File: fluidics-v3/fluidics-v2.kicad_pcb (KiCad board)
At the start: 4 copper layers, 85 x 95.5 mm, 83 parts, among them IC2 ADUM1250WSRZ-RL7, J1 PJ-063AH, J10 87832-0410, J11 0705430001, J12 87832-0410, J13 0705430001, J14 87832-0410, J15 0533980671, J16 0705430001, J17 0533980671, J18 87832-0410, J19 0705430001, J2 B6B-ZR-SM4-TF, J20 0533980671, J21 87832-0410, J22 0705430001, J24 0705430001, J25 87832-0410, J3 A-DS_15_A_KG-T4S, J4 B6B-ZR-SM4-TF, J5 Screw_Terminal_01x06, J6 Socket_1x24_2.54mm_SMT, J7 Socket_1x24_2.54mm_SMT, U1 TPL7407LDR, U11 MAX3221, U12 CD4050BDR, U13 TC7PZ17FU, U3 AP7366EA-33W5-7, U4 D24V10FX, U6 LTC4311CSC6-TRPBF

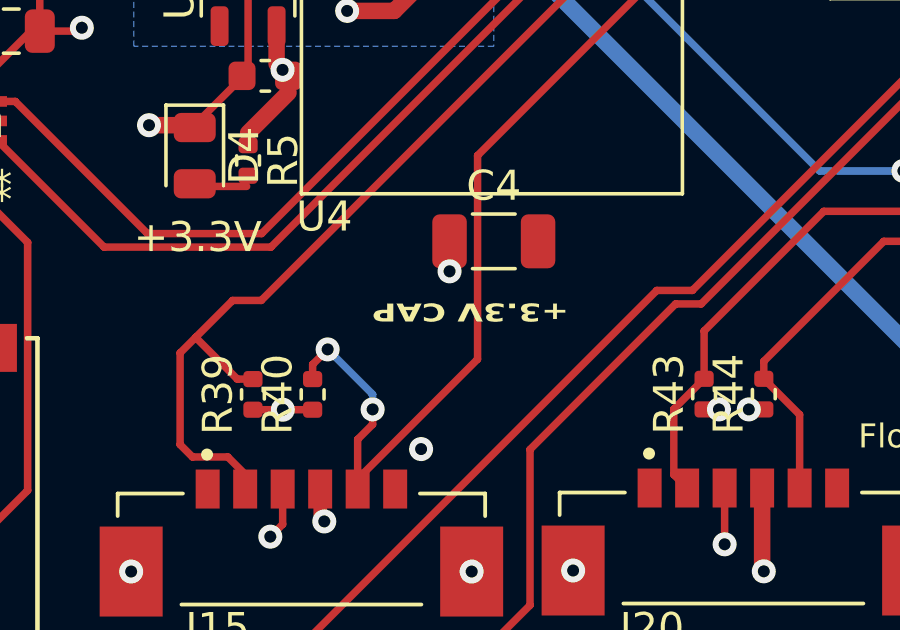
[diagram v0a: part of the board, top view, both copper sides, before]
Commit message: DNP the orphaned LTC4311, clean the CPL, fix undersized silk text
U6 (LTC4311 I2C accelerator) and R1 (0R) are vestigial from the accelerator
removal and cannot work as placed: pcbnew connectivity shows U6.1/U6.3 are the
only two of the twenty +5V pads unreachable from the buck output U4.5, and the
bus pins connect solely to each other -- Net-(U6-BUS1) = {U6.6, R1.1},
Net-(U6-BUS2) = {U6.4, R1.2}. Marked DNP on both the schematic (svalves sheet)
and the board rather than deleted, so the copper is left untouched and the
choice is reversible; deleting both is the cleaner fix for a future revision.

H2/H3/H4 (mounting holes) and TP1/TP2/TP3 (test points) are not placeable
parts but were being emitted into the placement file. Marked exclude-from-
position-files. Position export now also passes --exclude-dnp, so the CPL
drops from 82 to 74 rows and contains only parts a machine actually places.

Silk text "+3.3V CAP" was 0.8 x 0.6 mm against the board's own 0.8 mm silk
minimum; height raised to 0.8 mm. DRC text_height 1 -> 0, no other violation
moved.

Verified after the change: 44/44 socket pins still on the correct net, 4/4
intended no-connects, DRC unconnected 6 (unchanged baseline), schematic parity
0, 0 electrical violations, cosmetic 85 -> 84. Fab package regenerated.

Co-Authored-By: Claude Opus 5 (1M context) <noreply@anthropic.com>
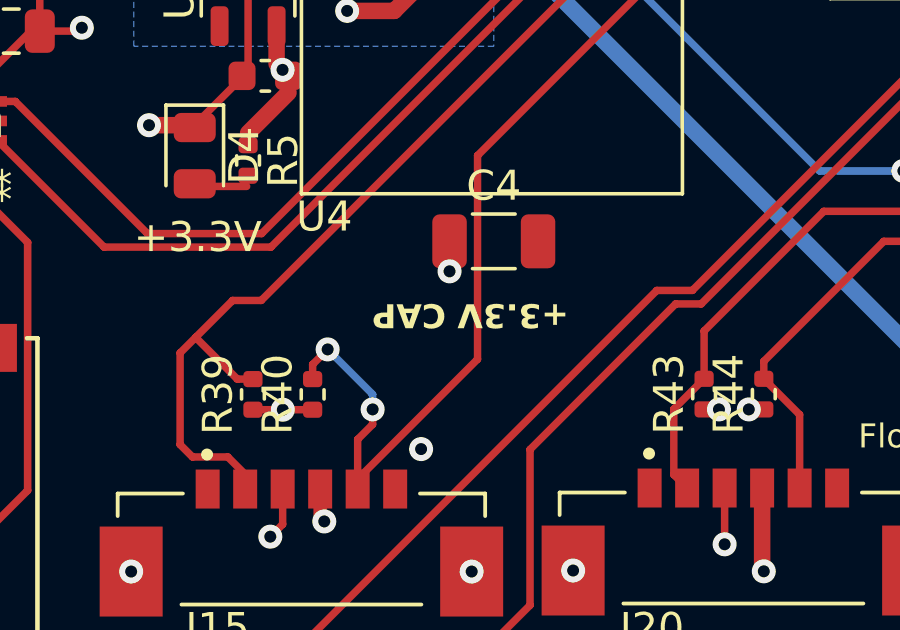
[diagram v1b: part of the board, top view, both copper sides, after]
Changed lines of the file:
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@@
 			)
 		)
+		(attr exclude_from_pos_files)
 		(duplicate_pad_numbers_are_jumpers no)
 		(fp_circle
@@
 			)
 		)
+		(attr exclude_from_pos_files)
 		(duplicate_pad_numbers_are_jumpers no)
 		(fp_circle
@@
 			)
 		)
+		(attr exclude_from_pos_files)
 		(duplicate_pad_numbers_are_jumpers no)
 		(fp_line
@@
 			)
 		)
-		(attr smd)
+		(attr smd dnp)
 		(duplicate_pad_numbers_are_jumpers no)
 		(fp_line
@@
 			)
 		)
+		(attr exclude_from_pos_files)
 		(duplicate_pad_numbers_are_jumpers no)
 		(fp_line
@@
 			)
 		)
-		(attr smd)
+		(attr smd dnp)
 		(duplicate_pad_numbers_are_jumpers no)
 		(fp_line
@@
 			)
 		)
+		(attr exclude_from_pos_files)
 		(duplicate_pad_numbers_are_jumpers no)
 		(fp_line
@@
 			)
 		)
+		(attr exclude_from_pos_files)
 		(duplicate_pad_numbers_are_jumpers no)
 		(fp_circle
@@
 		)
 	)
-	(gr_text "+3.3V CAP"
-		(at 159 92 180)
-		(layer "F.SilkS")
-		(effects
-			(font
-				(size 0.6 0.8)
-				(thickness 0.15)
-				(bold yes)
-			)
-			(justify left bottom)
-		)
-	)
 	(gr_text "Selector Valves"
 		(at 129 67 0)
@@
 		)
 	)
+	(gr_text "+3.3V CAP"
+		(at 159 92 180)
+		(layer "F.SilkS")
+		(effects
+			(font
+				(size 0.8 0.8)
+				(thickness 0.16)
+				(bold yes)
+			)
+			(justify left bottom)
+		)
+	)
 	(gr_text "J10"
 		(at 110.825 52 90)
@@
 	)
 	(segment
+		(start 184.2 60.22)
+		(end 187.5 60.22)
+		(width 0.25)
+		(layer "F.Cu")
+		(net "/POT_ANALOG")
+	)
+	(segment
 		(start 184.2 52.6)
 		(end 187.5 52.6)
@@
 		(net "/Bubble Sensors/Calib 1 5V")
 	)
-	(segment
-		(start 184.2 60.22)
-		(end 187.5 60.22)
-		(width 0.25)
-		(layer "F.Cu")
-		(net "/POT_ANALOG")
-	)
 	(zone

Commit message: Set socket MPN to Samtec SSM-124-L-SV
The land pattern was generated from Harwin's M20-786, but that series stops at
20 ways -- so no single Harwin part ever covered a row, and the board has never
had a one-part socket solution. Samtec's SSM-124-L-SV is a real 24-position
single-row 2.54mm SMT socket, and its footprint matches this land:

  tails         alternating          <- same
  offset        1.6025 mm            <- board has 1.65 mm, 47 um difference
  pad           1.905 x 1.02 mm      <- board has 1.9 x 1.0 mm
  pitch / span  2.54 / 58.42 mm      <- identical

Verified against the vendor footprint (SAMTEC_SSM-124-L-SV.kicad_mod). No
copper change: the tail sits 47 um off pad centre on a 1.9 mm pad. The
dual-land footprint is kept, so Harwin strips remain an alternative.

Value set on both the schematic and the board so BOM and CPL agree. Re-checked
after: 44/44 socket pins on the correct net, 4/4 intended no-connects, DRC
unconnected 6 (baseline), parity 0, 0 electrical violations. Fab package
regenerated.

Note: SSM-124-L-SV-P is the same socket with a pick-and-place pad, needed if
the sockets are to be machine placed rather than hand fitted. Only the plain
variant's land was verified here.

Co-Authored-By: Claude Opus 5 (1M context) <noreply@anthropic.com>
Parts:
- J6, J7: value Socket_1x24_2.54mm_SMT -> SSM-124-L-SV
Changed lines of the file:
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@@
 			)
 		)
-		(property "Value" "Socket_1x24_2.54mm_SMT"
+		(property "Value" "SSM-124-L-SV"
 			(at 0 32.08 0)
 			(layer "F.Fab")
@@
 			)
 		)
-		(property "Value" "Socket_1x24_2.54mm_SMT"
+		(property "Value" "SSM-124-L-SV"
 			(at 0 32.08 0)
 			(layer "F.Fab")

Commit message: U3: swap AP7366EA-33W5-7 -> AP2112K-3.3TRG1
Pin-compatible drop-in for the +3.3V LDO. Both parts are 600mA CMOS
LDOs with enable in SOT-23-5, and the fixed-output pin assignment is
identical (1=IN, 2=GND, 3=EN, 4=NC, 5=OUT), matching the board wiring
(+5V / GND / +5V / no-connect / +3.3V). Footprint unchanged
(Package_TO_SOT_SMD:SOT-23-5), so no layout impact.

Schematic, PCB and both BOMs updated together; schematic parity 0,
DRC 0 errors. Value text is on F.Fab only, so the existing gerbers and
positions.csv remain valid and were not regenerated.

Note: order the FIXED 3.3V variant. On the ADJ version pin 4 is the
feedback pin, not a no-connect.

Co-Authored-By: Claude Opus 5 (1M context) <noreply@anthropic.com>
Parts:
- U3: value AP7366EA-33W5-7 -> AP2112K-3.3TRG1
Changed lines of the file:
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@@
 			)
 		)
-		(property "Value" "AP7366EA-33W5-7"
+		(property "Value" "AP2112K-3.3TRG1"
 			(at 0 2.4 90)
 			(layer "F.Fab")

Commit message: U4: replace Pololu D24V10FX with Traco TSR1-2450E, drop 5V power-good
Swap the 24V->5V step-down for a Traco TSR 1-2450E (SIP-3, through-hole,
1A) using the stock KiCad symbol/footprint pair. The TSR is a 3-pin part,
so the Pololu's PG and nSHDN pins go away; nSHDN was already unconnected.

Schematic:
- psu: U4 -> Converter_DCDC:TSR1-2450E on
  Converter_DCDC:Converter_DCDC_TRACO_TSR1-xxxxE_THT
- Remove the PG-5V hierarchical label, sheet pin, wire stub and the 47k
  pull-up R51; PG-5V no longer exists as a net
- No-connect flags on J7 pin 1 and U2 pin 25, freeing Teensy pin 33

PCB:
- Place U4 at (156.437, 71.905) rot +90 so Vin lands on the existing +24V
  arrival node; GND and Vout follow on the 2.54mm pitch. Rotating rather
  than mirroring keeps the TSR body clear of R3 and D2, which the part
  would otherwise sit on top of.
- Route +5V on F.Cu 0.55mm from the existing tap across to Vout, plus a
  via restoring the F.Cu/B.Cu junction the old through-hole pad provided
- Remove orphaned PG-5V copper (16 segments, 2 vias) and the now-dead
  6-segment +3.3V run that used to feed R51

DRC: 0 errors, schematic parity clean, unconnected 7 -> 6.
Courtyard overlaps 2 -> 0, dangling tracks 4 -> 0. ERC 33 -> 31.
One cosmetic silkscreen warning remains: the "24V->5V Module" board label
now overlaps U4's outline and wants nudging by hand.

Co-Authored-By: Claude Opus 5 (1M context) <noreply@anthropic.com>
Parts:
- removed R51: 47k, Resistor_SMD:R_0603_1608Metric_Pad0.98x0.95mm_HandSolder
- U4: value D24V10FX -> TSR1-2450E; footprint pololu:D24V10FX -> Converter_DCDC:Converter_DCDC_TRACO_TSR1-xxxxE_THT
- moved U4 7.62 mm to (156.4, 71.9), turned to 90 degrees
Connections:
- J7 pad 1: /PG-5V -> unconnected-(J7-Pin_1-Pad1)
- U4 pad 1: /PG-5V -> +24V
- U4 pad 2: unconnected-(U4-nSHDN-Pad2) -> GND
- U4 pad 3: +24V -> +5V
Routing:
- net /PG-5V: track 49.0 -> 0.00 mm, vias 2 -> 0
- net +3.3V: track 68.6 -> 50.2 mm
- net +5V: track 99.1 -> 112.4 mm, vias 6 -> 7

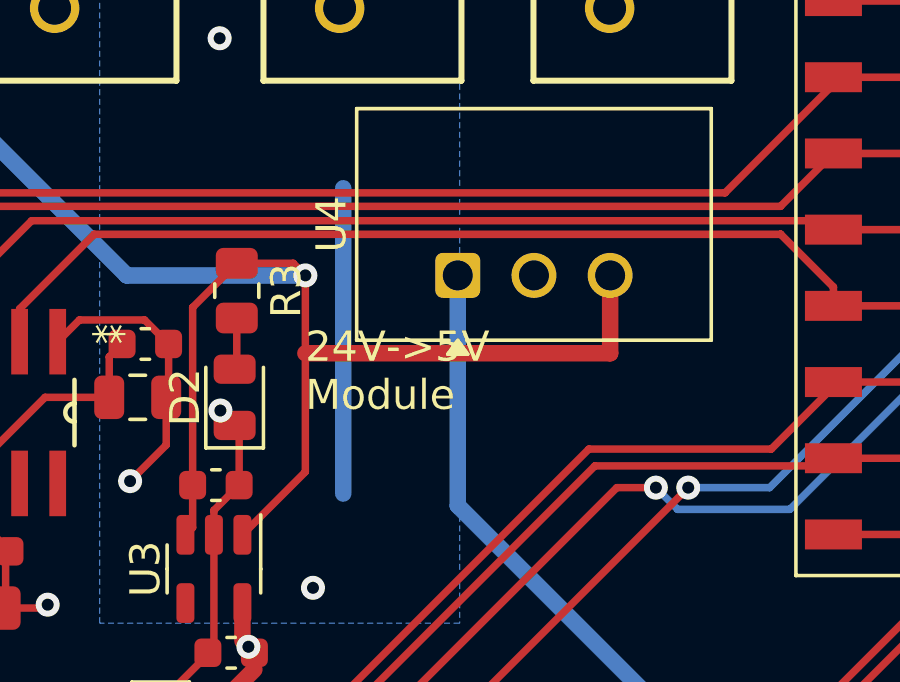
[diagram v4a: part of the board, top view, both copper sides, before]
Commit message: v3: finish TSR regulator swap, reconcile BOM, regenerate fab outputs
Follow-up to a773dae, which replaced the Pololu D24V10FX with a Traco
TSR 1-2450E. Completes the board cleanup and brings the fabrication
package back in step with the design.

Board:
- Remove the redundant B.Cu 3.3V spine at x=152.62; the 3V3_bridge_Bcu
  zone already carried that path, so connectivity is unchanged
- Move the "24V->5V Module" silk label clear of U4's outline
- R10 42K -> 47K. 42k is not an E24 value; R4 already uses 47k on the
  same +24V rail feeding an identical indicator LED, and the current
  difference is 0.52mA vs 0.47mA

DRC 0 errors, schematic parity clean, 6 unconnected items (all
pre-existing). Courtyard overlaps and dangling tracks both at 0.

Fabrication outputs, all regenerated from the current board:
- gerbers/ + drill (4-layer, metric 4.6, X2, merged PTH/NPTH), rezipped
- positions.csv, netlist.ipc, fluidics-v3.step

BOM and CPL:
- Add fluidics-v3-bom.xlsx, flattened from the EasyEDA template that
  broke JLC's importer: header moved to row 1, dropping five preamble
  rows, merged cells A1:D5, an embedded logo, =ROW() formulas whose
  cached values were lost on re-save, and four phantom trailing rows.
  Supplier Part renamed to "LCSC Part #" for auto-detection.
- Reconcile it against the board: add U4 (TSR 1-2450E, C5346721), drop
  R51 from the R10,R51 group (the PG pull-up died with the power-good
  net), correct U3 to AP2112K-3.3TRG1 / C51118 (was still the
  AP7366EA-33W5-7 part number from before 864ac36)
- Add cpl_jlcpcb.csv in JLCPCB column format
- Remove bom.csv: superseded, no LCSC column, and its range notation
  (C15-C17, R39-R44) is unparseable by JLC

BOM and CPL now agree exactly: 74 designators, 74 rows, no mismatch in
either direction, every line carrying an LCSC part number.

Co-Authored-By: Claude Opus 5 (1M context) <noreply@anthropic.com>
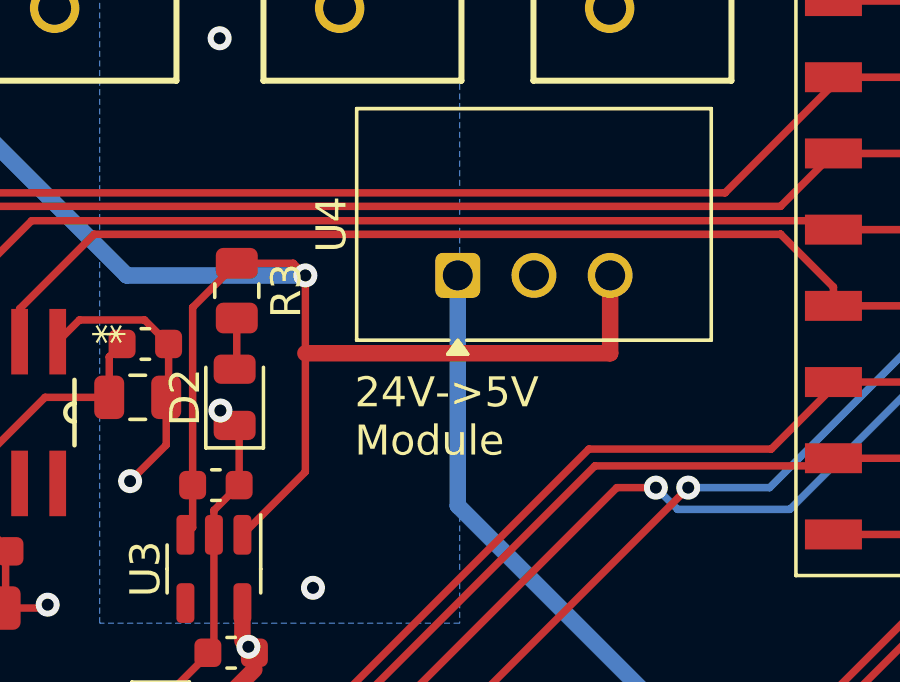
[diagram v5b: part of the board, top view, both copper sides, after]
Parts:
- R10: value 42K -> 47K
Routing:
- net +3.3V: track 50.2 -> 40.0 mm
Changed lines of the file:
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@@
 			)
 		)
-		(property "Value" "42K"
+		(property "Value" "47K"
 			(at 0 1.43 0)
 			(layer "F.Fab")
@@
 			(net "unconnected-(J7-Pin_1-Pad1)_1")
 			(pinfunction "Pin_1_1")
-			(pintype "passive")
+			(pintype "passive+no_connect")
 		)
 		(pad "1" smd rect
@@
 			(net "unconnected-(J7-Pin_1-Pad1)")
 			(pinfunction "Pin_1_1")
-			(pintype "passive")
+			(pintype "passive+no_connect")
 		)
 		(pad "2" smd rect
@@
 		)
 	)
-	(gr_text "24V->5V \nModule"
-		(at 151.35728 76.477 0)
+	(gr_text "+24V IN"
+		(at 153 37 0)
 		(layer "F.SilkS")
 		(effects
@@
 		)
 	)
-	(gr_text "+24V IN"
-		(at 153 37 0)
+	(gr_text "24V->5V \nModule"
+		(at 153 78 0)
 		(layer "F.SilkS")
 		(effects
@@
 		(net "+3.3V")
 	)
-	(segment
-		(start 152.61968 69)
-		(end 152.61968 79.17572)
-		(width 0.55)
-		(layer "B.Cu")
-		(net "+3.3V")
-	)
